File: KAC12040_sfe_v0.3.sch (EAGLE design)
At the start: 79 parts, among them IC2 93LC46ST, U2 TPD3E001DRLR, X1 332-12, X2 332-12, X3 52745-1690, X4 52745-1290

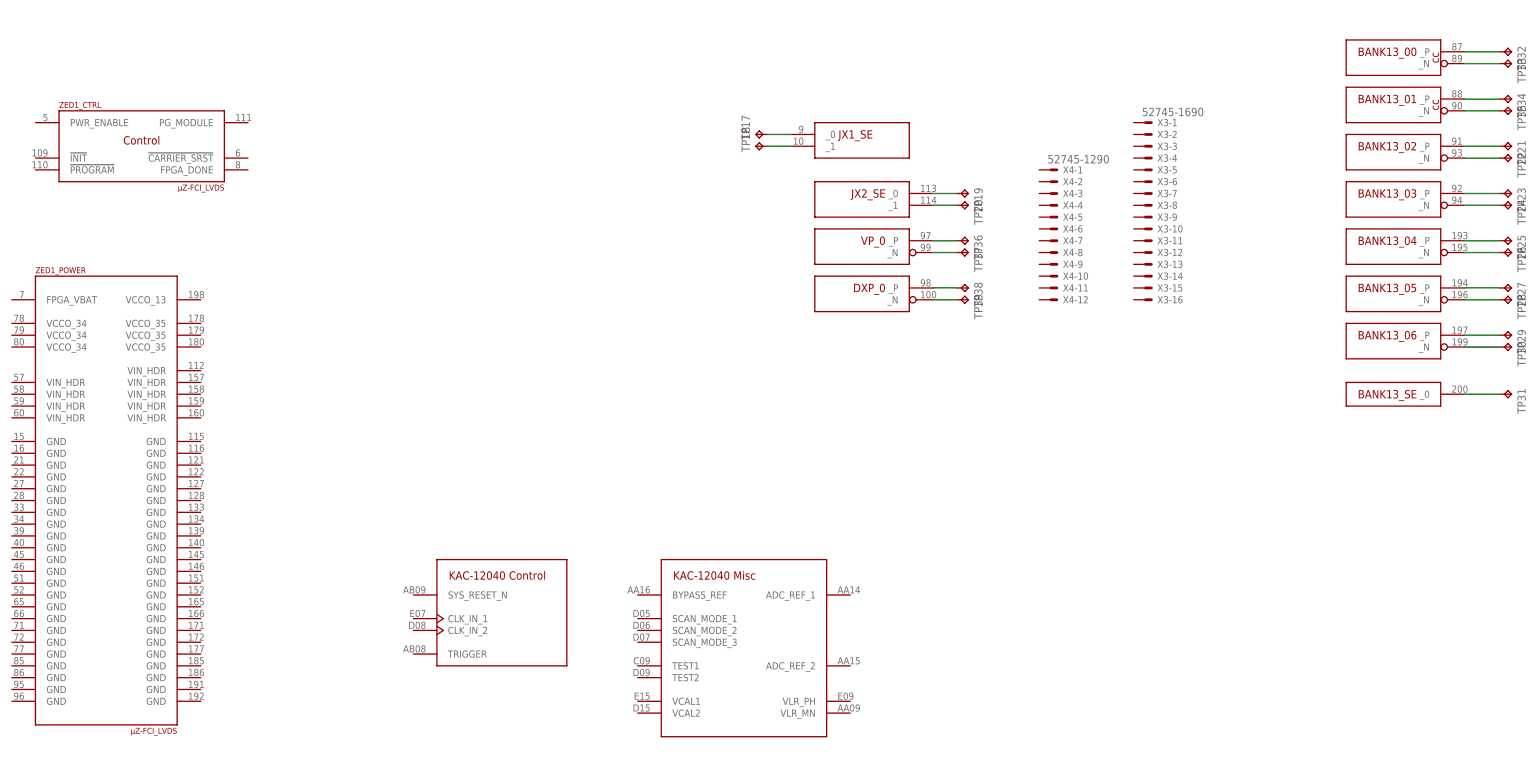
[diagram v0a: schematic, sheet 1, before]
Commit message: Basic power planes and vias
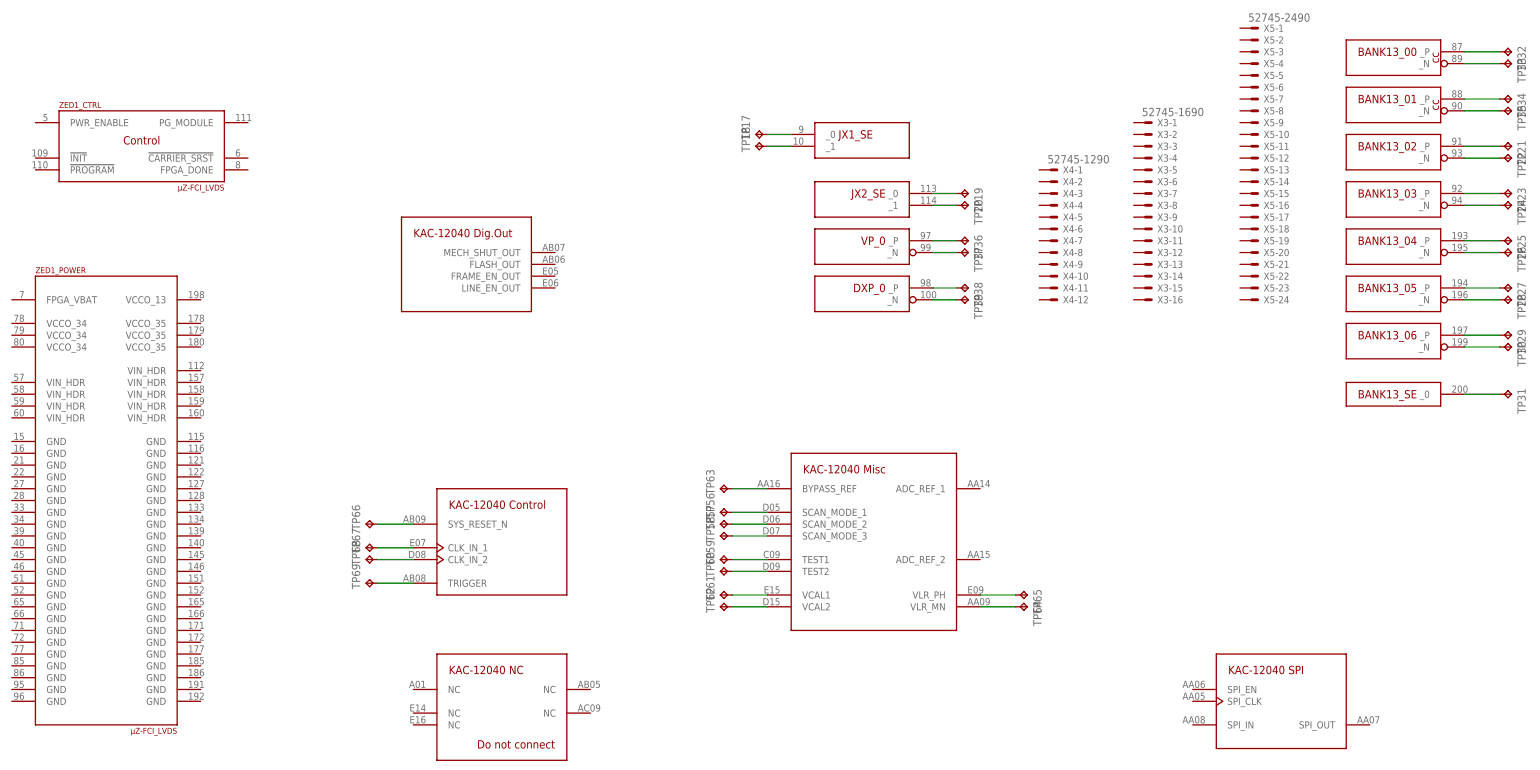
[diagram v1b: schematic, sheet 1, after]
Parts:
- added TP56, TP57, TP58, TP59, TP60, TP61, TP62, TP63, TP64, TP65: TPTP15SQ, testpad:TPTP15SQ
- added TP66, TP67, TP68, TP69: TPTP15R, testpad:TPTP15R
- added X5: 52745-2490, con-molex:52745-2490
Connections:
- net N$1 renamed VDD_DIG
- net N$2 renamed VREFP
- net N$3 renamed VSS_DIG
- net N$4 renamed AVDD_HV
- net N$65 renamed AVDD_LV
- net N$66 renamed AVSS_HV
- net N$67 renamed VDD_LVDS
- new net N$1: TP62.TP, U$1_MISC.VCAL2@D15
- new net N$2: TP61.TP, U$1_MISC.VCAL1@E15
- new net N$3: TP60.TP, U$1_MISC.TEST2@D09
- new net N$4: TP59.TP, U$1_MISC.TEST1@C09
- new net N$65: TP58.TP, U$1_MISC.SCAN_MODE_3@D07
- new net N$66: TP57.TP, U$1_MISC.SCAN_MODE_2@D06
- new net N$67: TP56.TP, U$1_MISC.SCAN_MODE_1@D05
- new net N$84: TP63.TP, U$1_MISC.BYPASS_REF@AA16
- new net N$85: TP65.TP, U$1_MISC.VLR_PH@E09
- new net N$86: TP64.TP, U$1_MISC.VLR_MN@AA09
- new net N$87: TP66.TP, U$1_CTRL.SYS_RESET_N@AB09
- new net N$88: TP67.TP, U$1_CTRL.CLK_IN_1@E07
- new net N$89: TP68.TP, U$1_CTRL.CLK_IN_2@D08
- new net N$90: TP69.TP, U$1_CTRL.TRIGGER@AB08

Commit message: Some minor updates
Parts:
- added U$3: IP4786CZ32SOT617-3, IP4786CZ32:IP4786CZ32SOT617-3
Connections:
- new net N$100: U$3G$1.S_DDAT, U$5_VIDEO.DDCSDA
- new net N$101: U$3G$1.S_HPD, U$5_VIDEO.HPD
- new net N$102: U$3G$1.S_CEC, U$5_VIDEO.CEC
- new net N$103: CN1G$1.CEC, U$3G$1.C_CEC
- new net N$104: CN1G$1.HOTPLUG, U$3G$1.C_HPD
- new net N$105: CN1G$1.DDAT, U$3G$1.C_DDAT
- new net N$106: CN1G$1.DCLK, U$3G$1.C_DCLK
- new net N$107: CN1G$1.TX2-, U$3G$1.C_TX2_N
- new net N$108: CN1G$1.TX2+, U$3G$1.C_TX2_P
- new net N$109: CN1G$1.TX1-, U$3G$1.C_TX1_N
- new net N$110: CN1G$1.TX1+, U$3G$1.C_TX1_P
- new net N$111: CN1G$1.TX0-, U$3G$1.C_TX0_N
- new net N$112: CN1G$1.TX0+, U$3G$1.C_TX0_P
- new net N$113: CN1G$1.TXC-, U$3G$1.C_C_N
- new net N$114: CN1G$1.TXC+, U$3G$1.C_C_P
- new net N$115: U$5_VIDEO.D0, U$5_VIDEO.D1, U$5_VIDEO.D10, U$5_VIDEO.D11, U$5_VIDEO.D12, U$5_VIDEO.D13, U$5_VIDEO.D14, U$5_VIDEO.D15, U$5_VIDEO.D2, U$5_VIDEO.D3, U$5_VIDEO.D4, U$5_VIDEO.D5, U$5_VIDEO.D6, U$5_VIDEO.D7, U$5_VIDEO.D8, U$5_VIDEO.D9
- new net N$116: U$5_VIDEO.D16, U$5_VIDEO.D17, U$5_VIDEO.D18, U$5_VIDEO.D19, U$5_VIDEO.D20, U$5_VIDEO.D21, U$5_VIDEO.D22, U$5_VIDEO.D23
- new net N$91: U$3G$1.S_C_P, U$5_VIDEO.TXC_P
- new net N$92: U$3G$1.S_C_N, U$5_VIDEO.TXC_N
- new net N$93: U$3G$1.S_TX0_P, U$5_VIDEO.TX0_P
- new net N$94: U$3G$1.S_TX0_N, U$5_VIDEO.TX0_N
- new net N$95: U$3G$1.S_TX1_P, U$5_VIDEO.TX1_P
- new net N$96: U$3G$1.S_TX1_N, U$5_VIDEO.TX1_N
- new net N$97: U$3G$1.S_TX2_P, U$5_VIDEO.TX2_P
- new net N$98: U$3G$1.S_TX2_N, U$5_VIDEO.TX2_N
- new net N$99: U$3G$1.S_DCLK, U$5_VIDEO.DDCSCL
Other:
- moved on the sheet: CN1, U$5_AUDIO, U$5_CTRL, U$5_VIDEO
